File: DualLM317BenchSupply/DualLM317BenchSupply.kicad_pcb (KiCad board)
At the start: 2 copper layers, 99.7 x 150.5 mm, 40 parts, among them CON101 BARREL_JACK, P101 CONN_1, P102 CONN_1, SW101 SPDT, SW102 SPDT, SW103 SPDT, SW201 SP6T, U101 78L05, U102 LM317, U103 LM317

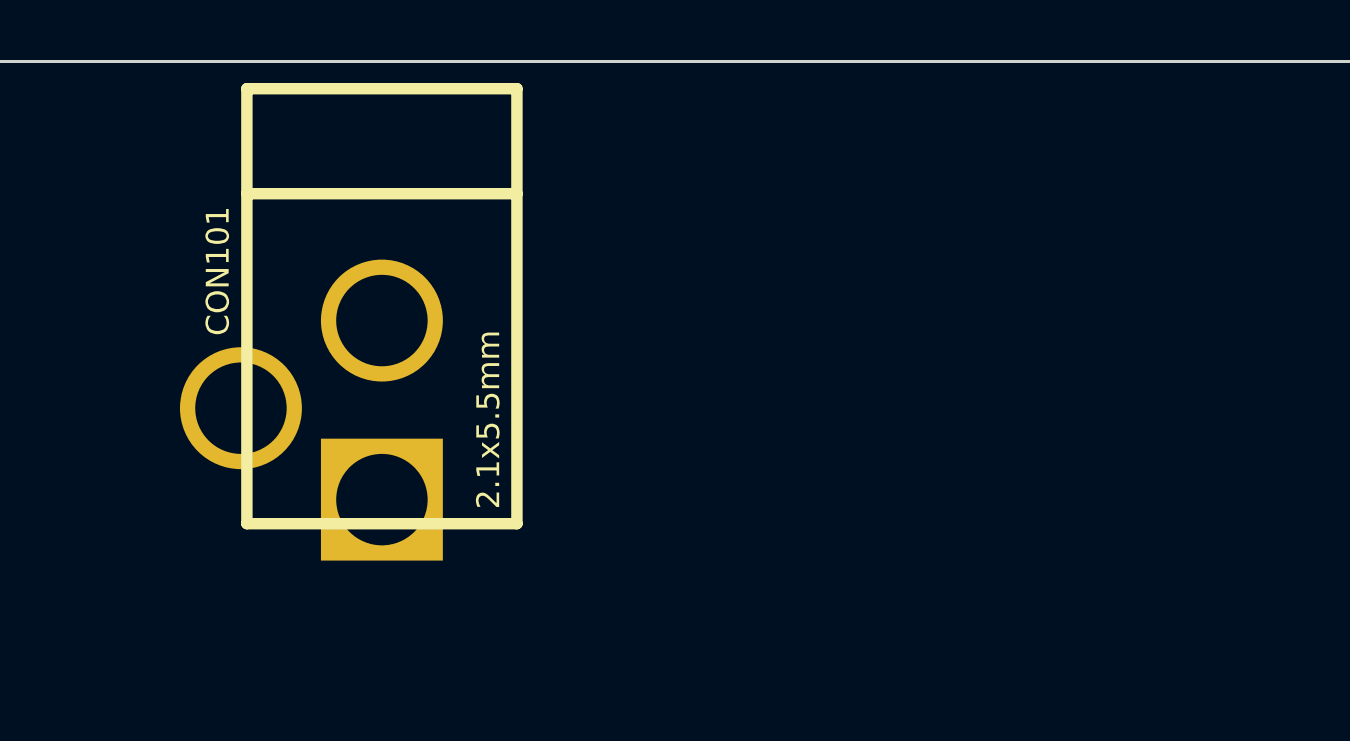
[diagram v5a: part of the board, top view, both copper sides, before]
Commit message: adding mounting holes to schematic
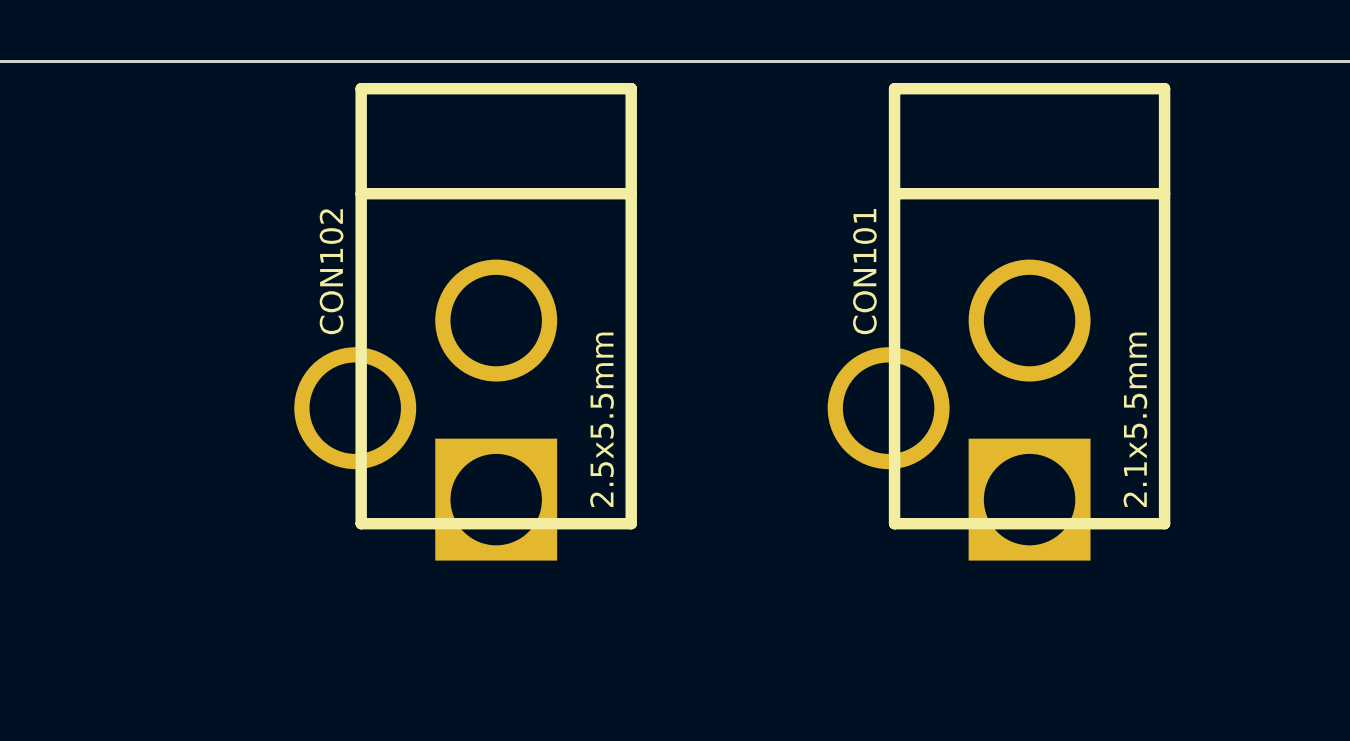
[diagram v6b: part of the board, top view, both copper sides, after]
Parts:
- added CON102: BARREL_JACK, BARREL_JACK_25x55, F.Cu at (158.8, 129.5)
- moved CON101 21.6 mm to (176.5, 129.5)

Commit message: dc jacks
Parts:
- removed H*** (x2): Val**, hole_M3
- added H101: HOLE, hole_M3, F.Cu at (139.7, 261.6)
- added H102: HOLE, hole_M3, F.Cu at (139.7, 118.1)
- added H103: HOLE, hole_M3, F.Cu at (232.4, 118.1)
- added H104: HOLE, hole_M3, F.Cu at (232.4, 261.6)
- moved SW103 48.1 mm to (261.6, 298.4)
- moved U101 46.4 mm to (262.9, 278.1)
- moved C107 38.4 mm to (252.7, 287.0)
- moved D101 37.0 mm to (250.2, 293.4)
- moved D103 37.0 mm to (270.5, 292.1)
- moved U103 33.2 mm to (293.4, 268.0)
- moved C104 26.2 mm to (283.2, 279.4)
- moved C105 26.2 mm to (275.6, 279.4)
- moved R101 21.1 mm to (269.2, 284.5)
- moved R102 21.1 mm to (283.2, 284.5)
- moved C101 18.8 mm to (252.7, 302.3)
- moved C106 18.8 mm to (261.6, 302.3)
- moved D104 17.6 mm to (280.7, 292.1)
- moved SW101 15.9 mm to (252.7, 298.4)
- moved U102 15.9 mm to (251.5, 278.1)
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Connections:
- P102 pad 1: (no net) -> N-0000018
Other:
- board size 99.7 x 150.5 mm -> 99.1 x 150.5 mm

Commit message: working on input layout
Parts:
- removed D101: 1N4148, LED_5MM
- removed D102, D104, D105: 1N4148, D3
- removed D103: LED, D3
- added C102: 0.1uF, C2, F.Cu at (257.8, 302.3)
- added H***: 530002B02500G, 530002B02500G, F.Cu at (186.1, 149.2)
- C101: value 100uF -> 1000uF; footprint C2 -> ELCAP_20_52_V
- C103: footprint C1V7 -> C2
- C104, C105, C107: footprint C1V7 -> ELCAP_10_20_V
- C106: footprint C2 -> ELCAP_10_20_V
- moved C101 192.3 mm to (146.1, 142.2)
- moved U103 165.3 mm to (189.9, 139.1), turned to 90 degrees
- moved U102 159.9 mm to (182.2, 134.0), turned to 270 degrees
- moved C106 57.1 mm to (281.9, 248.9)
- moved C107 44.3 mm to (273.1, 247.7)
- moved C105 34.9 mm to (294.6, 250.2)
- moved C103 33.2 mm to (266.7, 302.3)
- moved C104 33.1 mm to (255.3, 261.6)
- moved SW102 24.1 mm to (294.6, 298.4)
- moved DS102 14.0 mm to (275.6, 298.4)
- moved DS101 9.25 mm to (270.5, 281.9)
- moved R101 8.52 mm to (261.6, 288.3)
- moved R102 8.52 mm to (275.6, 288.3)
- moved U101 8.13 mm to (256.5, 283.2)
- moved RV101 5.08 mm to (284.5, 298.4)
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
